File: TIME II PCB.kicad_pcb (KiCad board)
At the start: 2 copper layers, 70 x 50 mm, 77 parts, among them J1 USB_C_Receptacle, J2 SD_Card, J4 Conn_01x06, J5 Conn_01x06, J6 Conn_01x06, J7 Conn_01x02_Male, J8 Conn_01x02_Male, Q1 VNP10N07, Q4 VNP10N07, Q5 VNP10N07, SW3 SW_SPDT, U2 ADP2303, U3 LTC4420CMSE-PBF, U7 STM32F103C8Tx, Y1 16 khz

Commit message: new board layout
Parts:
- removed C25, C27, C30: 100nF, Capacitor_SMD:C_0402_1005Metric
- removed C26: 10uF, Capacitor_SMD:C_0402_1005Metric
- removed C28, C29: 26pF, Capacitor_SMD:C_0402_1005Metric
- removed C7: 4.7 uF, Capacitor_SMD:C_0402_1005Metric
- removed D6: D, Diode_SMD:D_0402_1005Metric
- removed D7: D_Schottky, Diode_SMD:D_0603_1608Metric_Pad1.05x0.95mm_HandSolder
- removed L1: 2.2uH, inductor:IND_B1047AS-2R2N=P3
- removed MAX2: MAX17610, Package_DFN_QFN:WDFN-12-1EP_3x3mm_P0.45mm_EP1.7x2.5mm
- removed Q4, Q5: VNP10N07, Package_TO_SOT_SMD:SOT-23-3
- removed R23: 100k, Resistor_SMD:R_0402_1005Metric
- removed R24, R28: 300k, Resistor_SMD:R_0402_1005Metric
- removed R25: 154k, Resistor_SMD:R_0402_1005Metric
- removed R25.5: 2k, Resistor_SMD:R_0402_1005Metric
- removed R26: 45k, Resistor_SMD:R_0402_1005Metric
- removed R27, R30: 1M, Resistor_SMD:R_0402_1005Metric
- removed R29: 200k, Resistor_SMD:R_0402_1005Metric
- removed R31: 31.6k, Resistor_SMD:R_0402_1005Metric
- removed R32: 10.2k, Resistor_SMD:R_0402_1005Metric
- removed RSETI1: 1.8K, Resistor_SMD:R_0402_1005Metric
- removed SW3: SW_SPDT, Connector_PinHeader_1.27mm:PinHeader_1x03_P1.27mm_Vertical
- removed U7: STM32F103C8Tx, Package_QFP:LQFP-48_7x7mm_P0.5mm
- added C20: 2.2uF, Capacitor_SMD:C_0402_1005Metric, F.Cu at (97.4, 48.8)
- added C4: 100nF, Capacitor_SMD:C_0402_1005Metric, F.Cu at (113.7, 51.1)
- added F2: Fuse, Fuse:Fuse_0603_1608Metric, F.Cu at (94.0, 48.6)
- added J3: Conn_01x06, ffc_conn:CON_525590652_MOL, F.Cu at (105.3, 73.9)
- added Q2: VNP10N07, Package_TO_SOT_SMD:SOT-23-3, F.Cu at (118.7, 67.7)
- added Q3: VNP10N07, Package_TO_SOT_SMD:SOT-23-3, F.Cu at (107.4, 68.2)
- added R13: 45K, Resistor_SMD:R_0603_1608Metric, F.Cu at (95.1, 40.4)
- added R13.1: 154K, Resistor_SMD:R_0603_1608Metric, F.Cu at (95.1, 43.4)
- added R18: .33, Resistor_SMD:R_0402_1005Metric, F.Cu at (97.9, 67.1)
- added R19: 86.6K, Resistor_SMD:R_0402_1005Metric, F.Cu at (99.8, 46.0)
- added R5: 10k, Resistor_SMD:R_0402_1005Metric, F.Cu at (109.0, 53.5)
- added SW1: SW_SPDT, Connector_PinHeader_1.27mm:PinHeader_1x03_P1.27mm_Vertical, F.Cu at (104.0, 54.4)
- C1: value 10uF -> 100nF
- C10: value .1uF -> 26pF
- C11: value 2.2uF -> 26pF; moved to F.Cu
- C12, C14: value 47uF -> 10uF
- C13: value 15uF -> 0.01uF
- C15: value 10uF -> 0.01uF
- C16: value 0.01uF -> 15uF
- C17: value 100nF -> 2.2uF
- C18, C19: value 100nF -> 2.2pF
- C2: value 0.01uF -> 100nF
- C3, C5: value 2.2pF -> 100nF
- C6: value 0.47 uF -> 10nF
- C9: value 2.2uF -> 100nF
- J1: value USB_C_Receptacle -> SD_Card; footprint usb:USB4105-GF-A -> sdcardd:HZIP25-P-1
- J2: value SD_Card -> USB_C_Receptacle; footprint sdcard:MEM2075-00-140-01-A_GCT -> usb:USB4105-GF-A; moved to F.Cu
- J6: value Conn_01x06 -> Conn_01x02_Male; footprint ffc_conn:CON_525590652_MOL -> Connector_JST:JST_XH_B2B-XH-A_1x02_P2.50mm_Vertical
- J8: value Conn_01x02_Male -> Conn_01x02_Pin; footprint Connector_JST:JST_XH_B2B-XH-A_1x02_P2.50mm_Vertical -> Connector_JST:JST_XH_B2B-XH-AM_1x02_P2.50mm_Vertical
- Q1: moved to F.Cu
- R1: value .33 -> 1K
- R10, R12: value .33 -> 1M; moved to F.Cu
- R11: value 10k -> 2K; footprint Resistor_SMD:R_0402_1005Metric -> Resistor_SMD:R_0603_1608Metric
- R14: value 150K -> 576K
- R15: value .5 -> .33
- R16: value 15.2k -> .33
- R17: value 10.2k -> .33
- R2: value 100K -> 5.1k
- R3: value 1K -> 5.1k
- R4: value 100k -> 1K
- R6: value 5.1k -> 100K
- R7: value 5.1k -> 100k
- R8: value 1K -> 0.5
- R9: value .33 -> 300K; footprint Resistor_SMD:R_0402_1005Metric -> Resistor_SMD:R_0603_1608Metric
- U1: value ~ -> STM32F103C8Tx; footprint Package_DFN_QFN:WQFN-16-1EP_4x4mm_P0.5mm_EP2.6x2.6mm -> Package_QFP:LQFP-48_7x7mm_P0.5mm
- U2: value ADP2303 -> LTC4420CMSE-PBF; footprint Package_SO:SOIC-8-N7_3.9x4.9mm_P1.27mm -> Package_SO:MSOP-12-1EP_3x4mm_P0.65mm_EP1.65x2.85mm
- U3: value LTC4420CMSE-PBF -> ~; footprint Package_SO:MSOP-12-1EP_3x4mm_P0.65mm_EP1.65x2.85mm -> Package_DFN_QFN:WQFN-16-1EP_4x4mm_P0.5mm_EP2.6x2.6mm
- moved J7 123.2 mm to (87.9, 56.6), turned to -90 degrees
- moved R12 109.3 mm to (97.7, 46.0), turned to -90 degrees
- moved H1 106.3 mm to (87.6, 73.7), turned to 90 degrees
- moved U3 105.5 mm to (98.4, 55.9), turned to 0 degrees
- moved R8 103.1 mm to (96.5, 50.3), turned to 180 degrees
- moved R1 99.3 mm to (113.3, 42.7), turned to 0 degrees
- moved C3 99.1 mm to (115.6, 51.1)
- moved U2 97.7 mm to (101.4, 41.8)
- moved D2 97.6 mm to (110.0, 45.0), turned to 0 degrees
- moved C14 97.3 mm to (100.1, 50.7), turned to -90 degrees
- moved C2 95.6 mm to (117.6, 51.1), turned to -90 degrees
- moved C1 94.4 mm to (119.6, 51.1), turned to -90 degrees
- moved C17 93.8 mm to (94.2, 50.8)
- moved C12 93.2 mm to (104.0, 50.7), turned to -90 degrees
- moved U1 92.7 mm to (113.0, 59.2), turned to 0 degrees
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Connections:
- C1 pad 1: 5v -> 3v3
- C10 pad 1: 5v -> GND
- C10 pad 2: Net-(D7-K) -> Net-(U1-PD0)
- C11 pad 1: BAT -> GND
- C11 pad 2: GND -> Net-(U1-PD1)
- C12 pad 1: 3v3 -> USB_P
- C13 pad 1: 5v -> USB_P
- C13 pad 2: GND -> Net-(U3-VCP)
- C14 pad 1: 3v3 -> USB_P
- C15 pad 1: 5v -> USB_P
- C15 pad 2: GND -> Net-(U4-VCP)
- C16 pad 1: 5v -> HEAT_POW
- C16 pad 2: Net-(U4-VCP) -> GND
- C17 pad 1: 3v3 -> Net-(C17-Pad1)
- C18 pad 1: 3v3 -> Net-(U3-VINT)
- C19 pad 1: 3v3 -> Net-(U4-VINT)
- C2 pad 1: 5v -> 3v3
- C2 pad 2: Net-(U1-VCP) -> GND
- C3 pad 1: Net-(U1-VINT) -> 3v3
- C5 pad 1: Net-(U4-VINT) -> 3v3
- C6 pad 1: USB_P -> 3v3
- C8 pad 1: 5v -> 3v3
- C9 pad 1: Net-(C9-Pad1) -> /nrst
- J4 pad 2: therm_1 -> therm_3
- J6 pad 1: 5v -> MOTOR_1A
- J6 pad 2: therm_3 -> MOTOR_1
- J8 pad 1: MOTOR_1A -> BAT_REAL
- J8 pad 2: MOTOR_1 -> GND
- Q1 pad 1: heater_2 -> heater_1
- Q1 pad 2: Net-(J5-Pin_6) -> Net-(J3-Pin_6)
- R1 pad 1: Net-(U1-BISEN) -> LED
- R1 pad 2: GND -> Net-(D1-A)
- R10 pad 1: Net-(U4-BISEN) -> HEAT_POW
- R10 pad 2: GND -> Net-(U2-CMPOUT1)
- R11 pad 2: Net-(U7-BOOT0) -> Net-(U2-ADJ)
- R12 pad 1: Net-(U1-AISEN) -> HEAT_POW
- R12 pad 2: GND -> Net-(U2-V2OK)
- R14 pad 1: Net-(MAX2-CLMODE) -> BAT
- R14 pad 2: GND -> Net-(U2-V2UV)
- R15 pad 1: 5v -> Net-(U3-BISEN)
- R15 pad 2: Net-(C9-Pad1) -> GND
- R16 pad 1: 5v -> Net-(U3-AISEN)
- R16 pad 2: Net-(U2-EN) -> GND
- R17 pad 1: Net-(U2-EN) -> Net-(U4-BISEN)
- R2 pad 1: BAT_REAL -> Net-(J2-CC1)
- R2 pad 2: V_MON -> GND
- R3 pad 1: LED -> Net-(J2-CC2)
- R3 pad 2: Net-(D1-A) -> GND
- R4 pad 1: V_MON -> 3v3
- R4 pad 2: GND -> Net-(D2-A)
- R6 pad 1: Net-(J1-CC1) -> BAT_REAL
- R6 pad 2: GND -> V_MON
- R7 pad 1: Net-(J1-CC2) -> V_MON
- R8 pad 1: 3v3 -> USB_P
- R8 pad 2: Net-(D2-A) -> Net-(C17-Pad1)
- R9 pad 1: Net-(U4-AISEN) -> USB_P
- R9 pad 2: GND -> Net-(U2-ADJ)
- U1 pad 1: MOT_CON2 -> 3v3
- U1 pad 10: SERVO_2A -> therm_2
- U1 pad 11: Net-(U1-VCP) -> heater_1
- U1 pad 12: 5v -> therm_1
- U1 pad 13: GND -> SERVO_2A
- U1 pad 14: Net-(U1-VINT) -> MOT_CON2
- U1 pad 15: SERVO_2A -> MOT_MON_2
- U1 pad 17: GND -> unconnected-(U1-PA7-Pad17)
- U1 pad 2: MOTOR_2 -> unconnected-(U1-PC13-Pad2)
- U1 pad 3: Net-(U1-AISEN) -> unconnected-(U1-PC14-Pad3)
- U1 pad 4: MOTOR_2A -> unconnected-(U1-PC15-Pad4)
- U1 pad 5: MOTOR_2A -> Net-(U1-PD0)
- U1 pad 6: Net-(U1-BISEN) -> Net-(U1-PD1)
- U1 pad 7: MOTOR_2 -> /nrst
- U1 pad 8: MOT_MON_2 -> GND
- U1 pad 9: SERVO_2 -> Net-(U1-VDDA)
- U2 pad 1: 5v -> USB_P
- U2 pad 2: 5v -> HEAT_POW
- U2 pad 3: Net-(U2-EN) -> Net-(U2-CMP1)
- U2 pad 4: Net-(U2-PGOOD) -> Net-(U2-ADJ)
- U2 pad 5: Net-(U2-FB) -> GND
- U2 pad 6: unconnected-(U2-NC-Pad6) -> Net-(U2-CMPOUT1)
- U2 pad 8: Net-(D7-K) -> Net-(U2-V2OK)
- U3 pad 1: 5v -> MOT_CON2
- U3 pad 10: 5v -> SERVO_2A
- U3 pad 11: GND -> Net-(U3-VCP)
- U3 pad 12: BAT -> USB_P
- U3 pad 2: unconnected-(U3-V2TEST-Pad2) -> MOTOR_2
- U3 pad 3: Net-(U3-CMP1) -> Net-(U3-AISEN)
- U3 pad 4: Net-(U3-ADJ) -> MOTOR_2A
- U3 pad 5: GND -> MOTOR_2A
- U3 pad 6: Net-(U3-CMPOUT1) -> Net-(U3-BISEN)
- U3 pad 7: Net-(U3-GNDSW) -> MOTOR_2
- U3 pad 8: Net-(U3-CMPOUT1) -> MOT_MON_2
- U3 pad 9: 5v -> SERVO_2
- U4 pad 12: 5v -> USB_P
- Y1 pad 1: Net-(U7-PD1) -> Net-(U1-PD1)
- Y1 pad 2: Net-(U7-PD0) -> Net-(U1-PD0)
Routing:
- net 5v: track 253.7 -> 23.4 mm, vias 6 -> 0
- net GND: track 84.0 -> 0.03 mm, vias 7 -> 0
- net 3v3: track 105.0 -> 35.1 mm
- net Net-(U4-VCP): track 2.57 -> 50.8 mm, vias 0 -> 3
- net USB_P: track 4.86 -> 49.0 mm, vias 0 -> 2
- net Net-(U1-PD1): track 0.00 -> 43.7 mm, vias 0 -> 5
- net heater_1: track 23.0 -> 64.7 mm, vias 1 -> 2
- net heater_2: track 27.1 -> 64.9 mm, vias 1 -> 2
- net therm_2: track 42.2 -> 77.2 mm, vias 3 -> 7
- net HEAT_POW: track 0.00 -> 32.3 mm, vias 0 -> 2
- net Net-(U4-VINT): track 1.81 -> 33.7 mm, vias 0 -> 6
- net Net-(J5-Pin_6): track 5.69 -> 32.7 mm, vias 1 -> 3
- net BAT_REAL: track 2.66 -> 27.1 mm, vias 0 -> 2
- net V_MON: track 13.6 -> 35.4 mm, vias 0 -> 2
- net Net-(U2-GNDSW): track 0.00 -> 20.1 mm, vias 0 -> 2
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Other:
- board outline removed
- board text removed: "+"
- board text removed: "-"

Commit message: major reroute
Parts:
- removed J1: SD_Card, sdcardd:HZIP25-P-1
- Q1, Q2, Q3, R2, R3, R5: moved to B.Cu
- moved R7 21.5 mm to (124.0, 52.6), turned to -90 degrees
- moved D1 19.8 mm to (128.7, 49.2), turned to -90 degrees
- moved R1 18.1 mm to (128.6, 52.5), turned to 90 degrees
- moved R6 18.0 mm to (124.0, 49.1), turned to -90 degrees
- moved D2 17.2 mm to (126.6, 49.2), turned to -90 degrees
- moved SW1 16.7 mm to (120.5, 56.5), turned to 180 degrees
- moved R4 15.2 mm to (126.6, 52.6), turned to 90 degrees
- moved Y1 14.8 mm to (105.7, 54.4)
- moved C8 13.5 mm to (121.2, 50.0), turned to 90 degrees
- moved C19 13.3 mm to (94.0, 53.0), turned to 180 degrees
- moved C1 12.8 mm to (106.8, 50.0), turned to 90 degrees
- moved C18 11.9 mm to (102.5, 65.0)
- moved R18 11.3 mm to (94.0, 56.5), turned to 180 degrees
- moved R3 10.9 mm to (119.5, 39.0)
- moved Q3 10.8 mm to (98.7, 74.6), turned to 90 degrees
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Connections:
- U1 pad 10: therm_2 -> MOT_CON2
- U1 pad 11: heater_1 -> SERVO_2
- U1 pad 12: therm_1 -> SERVO_2A
- U1 pad 13: SERVO_2A -> MOT_MON_2
- U1 pad 14: MOT_CON2 -> therm_2
- U1 pad 15: MOT_MON_2 -> heater_2
- U1 pad 16: SERVO_2 -> therm_1
- U1 pad 17: unconnected-(U1-PA7-Pad17) -> heater_1
- U1 pad 18: V_MON -> therm_3
- U1 pad 19: therm_3 -> heater_3
- U1 pad 2: unconnected-(U1-PC13-Pad2) -> MOT_MON_1
- U1 pad 29: heater_3 -> unconnected-(U1-PA8-Pad29)
- U1 pad 40: MOT_MON_1 -> unconnected-(U1-PB4-Pad40)
- U1 pad 45: heater_2 -> unconnected-(U1-PB8-Pad45)
- U1 pad 46: unconnected-(U1-PB9-Pad46) -> V_MON
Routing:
- net therm_2: track 77.2 -> 22.5 mm, vias 7 -> 0
- net heater_1: track 64.7 -> 12.9 mm, vias 2 -> 1
- net Net-(U4-VCP): track 50.8 -> 9.12 mm, vias 3 -> 2
- net heater_2: track 64.9 -> 31.2 mm, vias 2 -> 1
- net Net-(U1-PD1): track 43.7 -> 10.2 mm, vias 5 -> 2
- net GND: track 0.03 -> 27.0 mm, vias 0 -> 14
- net Net-(U4-VINT): track 33.7 -> 7.09 mm, vias 6 -> 2
- net Net-(J5-Pin_6): track 32.7 -> 7.28 mm, vias 3 -> 1
- net MOT_CON2: track 32.7 -> 10.5 mm, vias 2 -> 0
- net Net-(U3-VCP): track 5.52 -> 24.3 mm, vias 0 -> 2
- net MISO: track 18.1 -> 0.00 mm, vias 2 -> 0
- net Net-(U2-GNDSW): track 20.1 -> 2.79 mm, vias 2 -> 0
- net MOTOR_1: track 33.4 -> 17.0 mm, vias 5 -> 2
- net V_MON: track 35.4 -> 19.6 mm
- net USB_P: track 49.0 -> 63.8 mm, vias 2 -> 5
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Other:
- board outline added: 46 x 41.8 mm

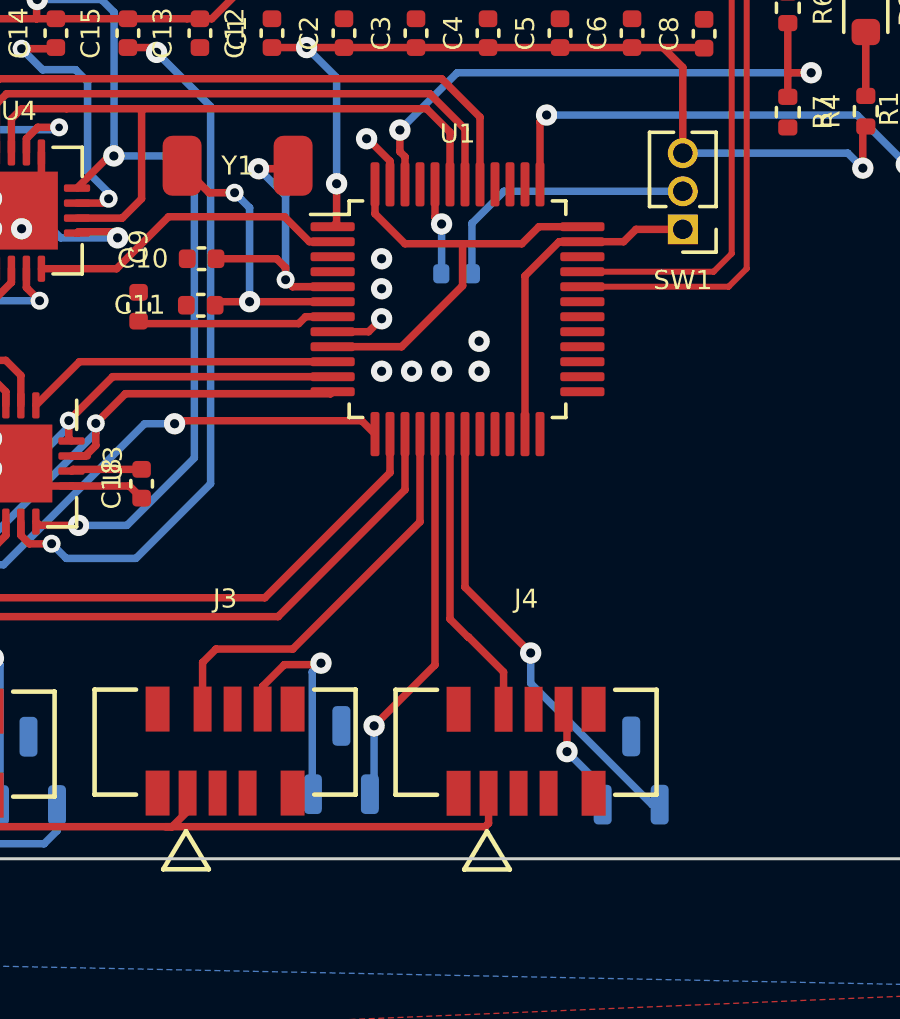
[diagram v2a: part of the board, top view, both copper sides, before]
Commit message: ldo added back
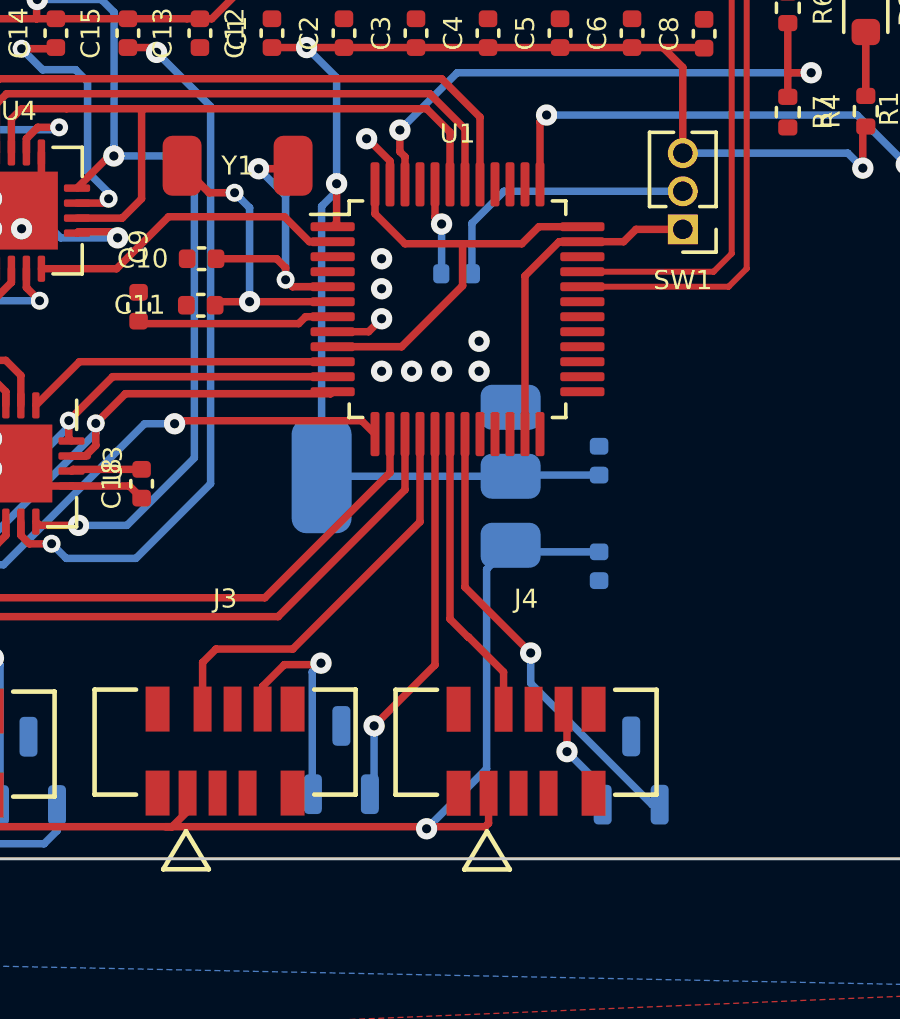
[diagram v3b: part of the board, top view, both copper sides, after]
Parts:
- added C21: 22 uF, Capacitor_SMD:C_0402_1005Metric, B.Cu at (117.8, 64.2)
- added C7: 10 uF, Capacitor_SMD:C_0402_1005Metric, B.Cu at (117.8, 67.8)
- added U5: AMS1117-3.3, Package_TO_SOT_SMD:SOT-223-3_TabPin2, B.Cu at (111.7, 64.8)
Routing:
- net 3v3: track 32.3 -> 51.5 mm
- net 5v: track 23.5 -> 37.1 mm, vias 0 -> 1

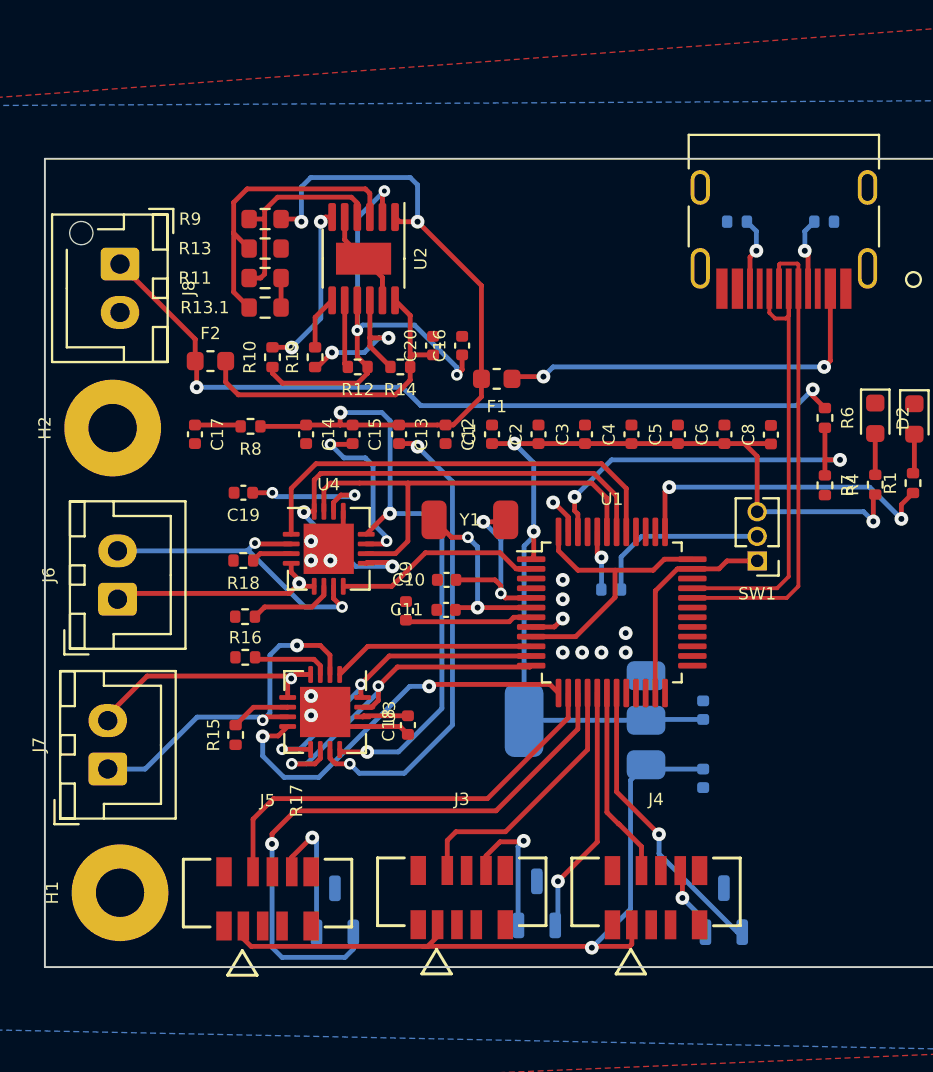
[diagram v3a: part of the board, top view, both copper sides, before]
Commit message: thicker power rails
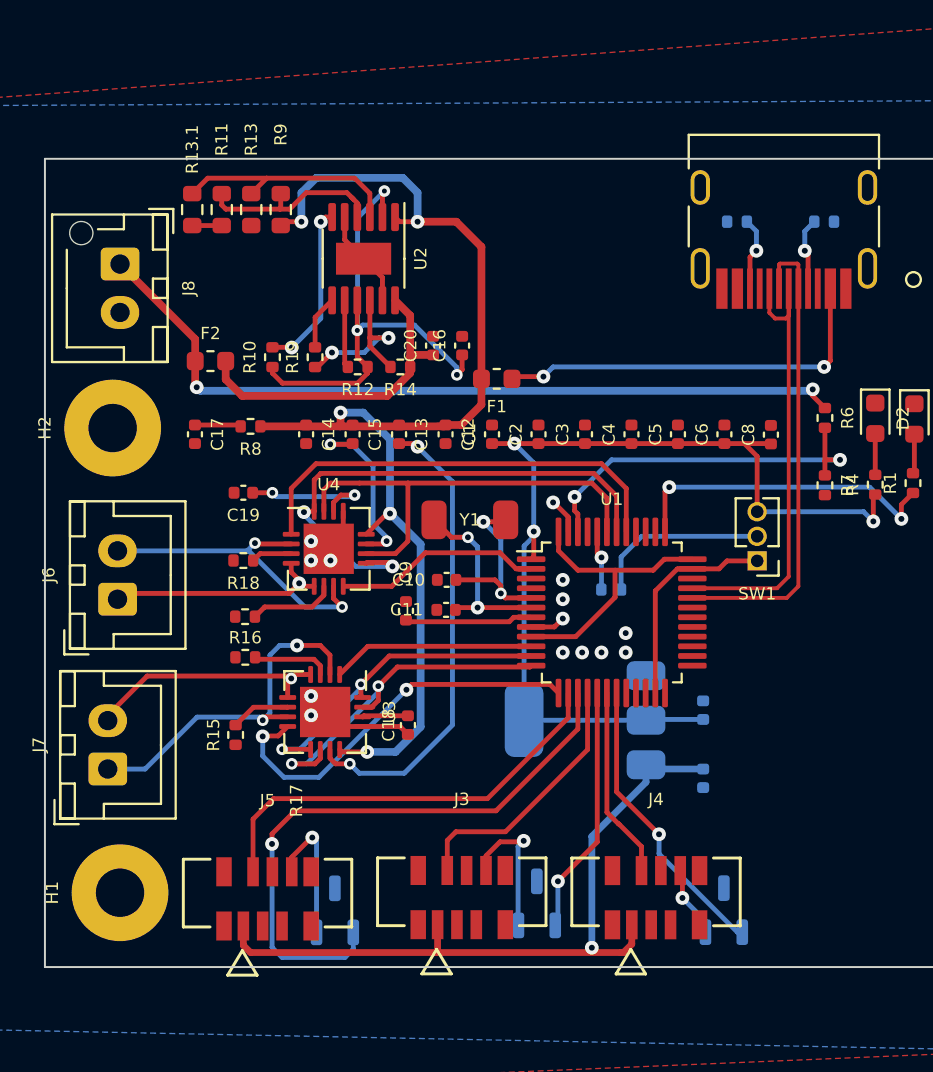
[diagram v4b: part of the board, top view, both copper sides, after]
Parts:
- moved R13.1 6.31 mm to (91.4, 38.4), turned to -90 degrees
- moved R11 4.19 mm to (92.9, 38.4), turned to 90 degrees
- moved R13 2.14 mm to (94.4, 38.4), turned to -90 degrees
- moved R9 0.95 mm to (95.9, 38.4), turned to 90 degrees
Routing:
- net Net-(U2-CMP1): track 15.5 -> 12.2 mm
- net 5v: track 37.1 -> 38.9 mm
- net Net-(U2-ADJ): track 10.9 -> 9.93 mm
- net BAT_REAL: track 41.8 -> 41.3 mm

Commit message: Update README
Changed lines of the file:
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@@
 		(polygon
 			(pts
-				(xy 79 32.75) (xy 76.5 84.25) (xy 135.75 81.75) (xy 133.5 28.75)
+				(xy 74.5 28.75) (xy 71 85) (xy 140.75 85.75) (xy 137.25 26.25)
 			)
 		)

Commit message: week of 01/10/24
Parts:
- added J1: SD_Card, 114_00841_68:AMPHENOL_1140084168, F.Cu at (121.3, 67.9)
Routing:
- net MISO: track 0.00 -> 19.1 mm
- net 3v3: track 51.5 -> 68.0 mm
- net SS: track 0.00 -> 10.0 mm
- net SCK: track 0.00 -> 7.72 mm
- net MOSI: track 0.00 -> 6.29 mm
